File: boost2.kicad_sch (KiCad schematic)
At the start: 26 parts, among them Q6 BSC015NE2LS5I, Q7 BSC015NE2LS5I, U1 TPS43061

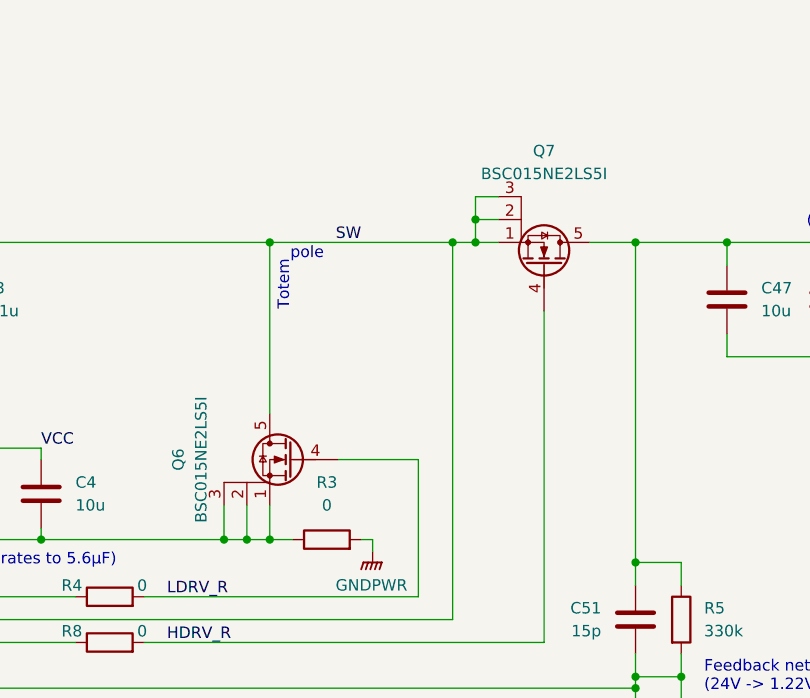
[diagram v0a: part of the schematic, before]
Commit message: Up charging current to 6A
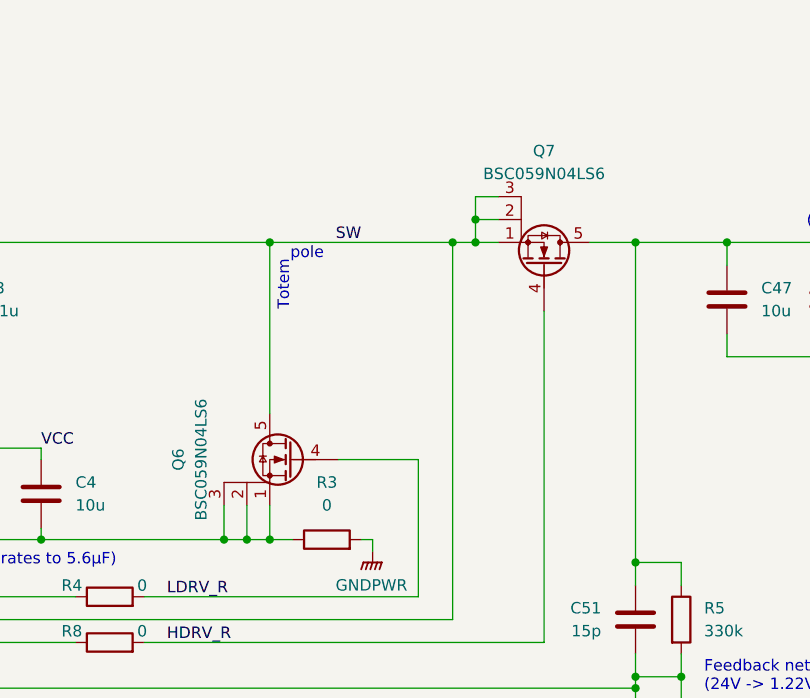
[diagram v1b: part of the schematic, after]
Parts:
- Q6, Q7: value BSC015NE2LS5I -> BSC059N04LS6; Mouser Part Number 726-BSC015NE2LS5IATM -> 726-BSC059N04LS6ATMA
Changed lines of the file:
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@@
 			)
 		)
-		(property "Value" "BSC015NE2LS5I"
+		(property "Value" "BSC059N04LS6"
 			(at 139.7 102.87 90)
 			(effects
@@
 			)
 		)
-		(property "Mouser Part Number" "726-BSC015NE2LS5IATM"
+		(property "Mouser Part Number" "726-BSC059N04LS6ATMA"
 			(at 149.86 102.87 0)
 			(effects
@@
 			)
 		)
-		(property "Value" "BSC015NE2LS5I"
+		(property "Value" "BSC059N04LS6"
 			(at 177.8 71.12 90)
 			(effects
@@
 			)
 		)
-		(property "Mouser Part Number" "726-BSC015NE2LS5IATM"
+		(property "Mouser Part Number" "726-BSC059N04LS6ATMA"
 			(at 177.8 81.28 0)
 			(effects

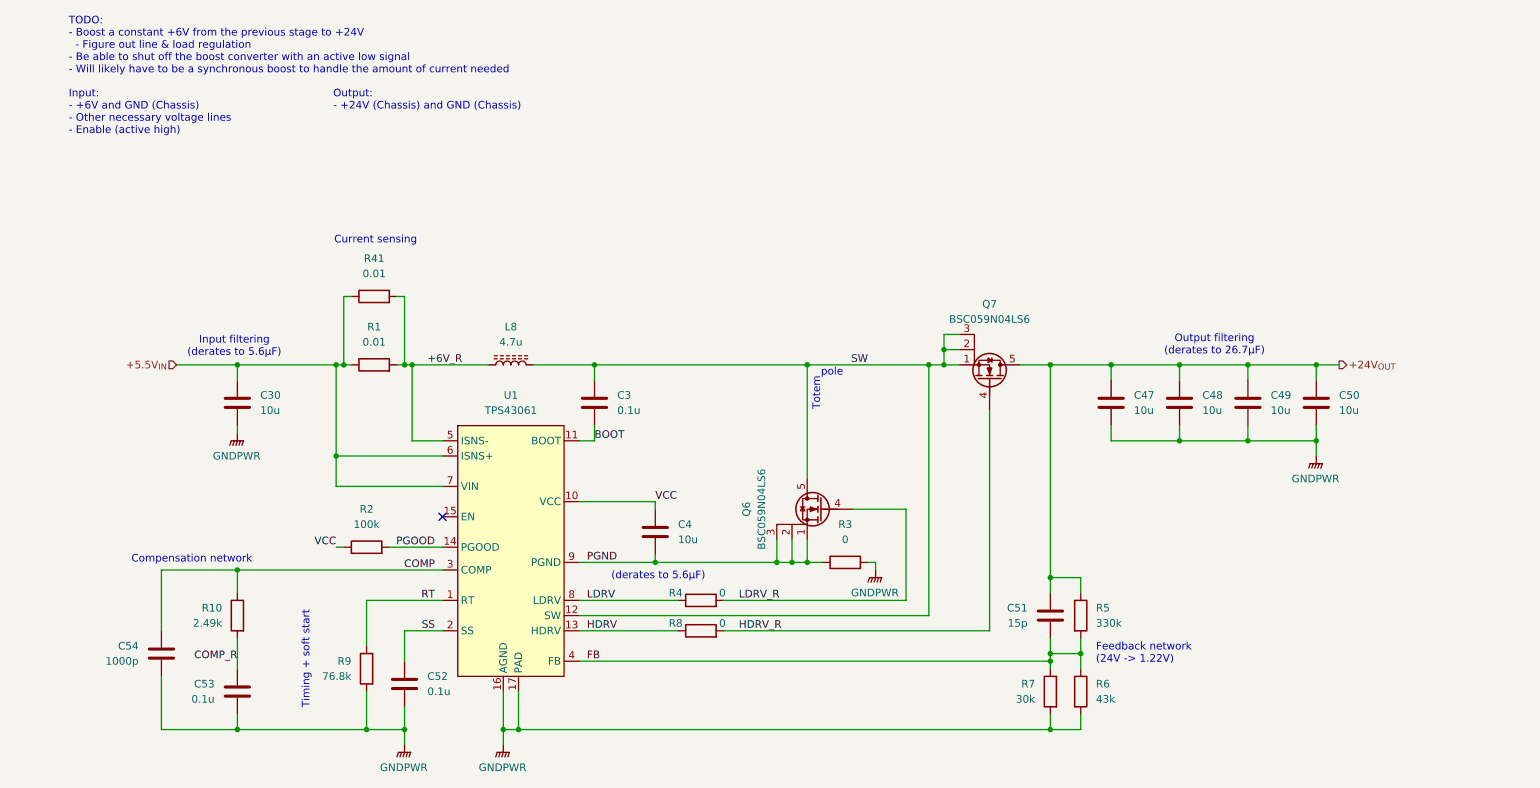
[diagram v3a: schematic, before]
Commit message: Reannotate schematic
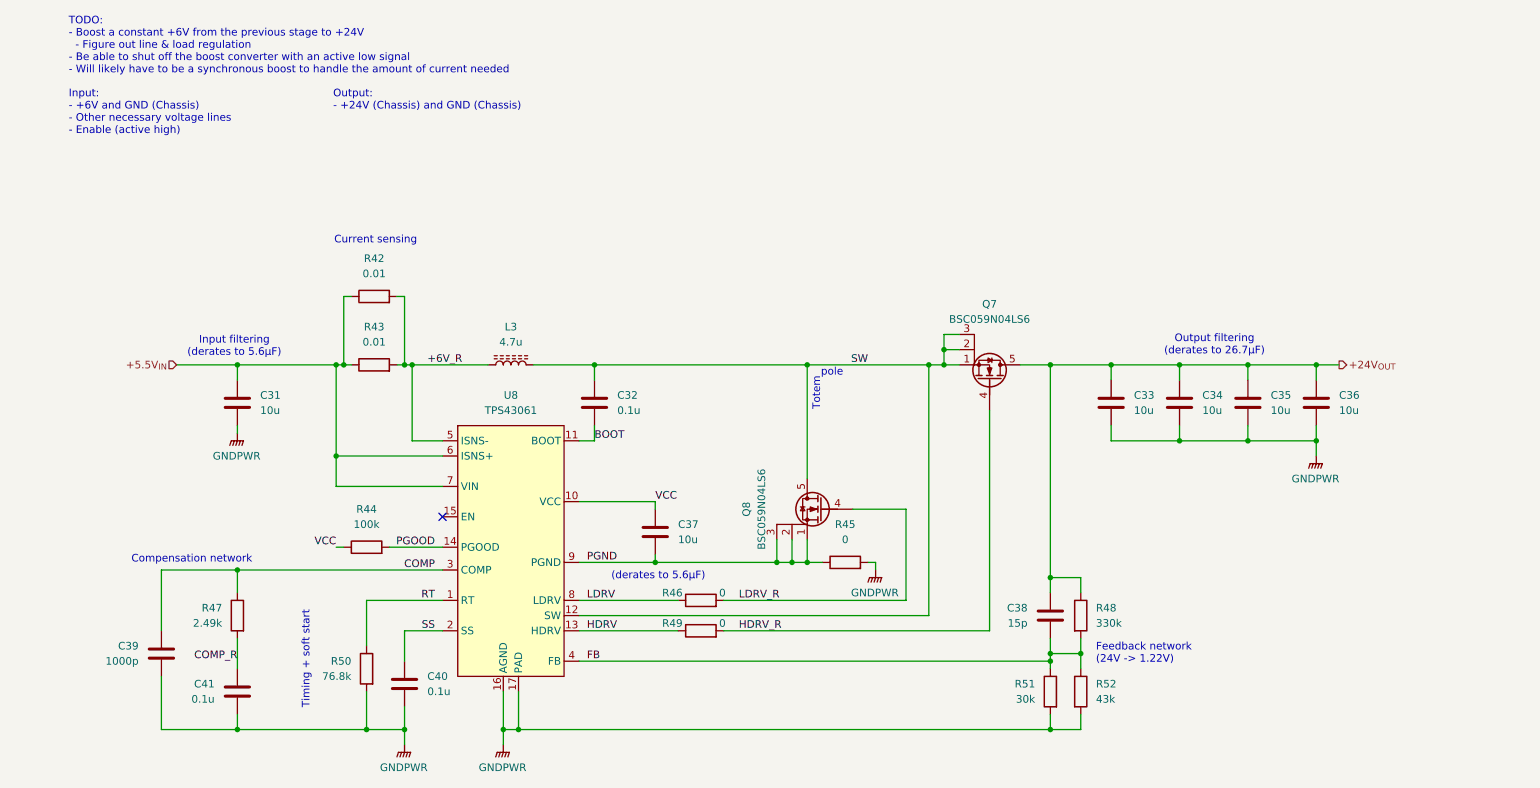
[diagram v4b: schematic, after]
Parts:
- renumbered C30 to C31, C3 to C32, C47 to C33, C48 to C34, C49 to C35, C50 to C36, C4 to C37, C51 to C38, C54 to C39, C52 to C40, C53 to C41, L8 to L3, Q6 to Q8, R41 to R42, R1 to R43, R2 to R44, R3 to R45, R4 to R46, R10 to R47, R5 to R48, R8 to R49, R9 to R50, R7 to R51, R6 to R52, U1 to U8
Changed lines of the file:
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@@
 		(dnp no)
 		(fields_autoplaced yes)
-		(property "Reference" "R3"
+		(property "Reference" "R45"
 			(at 153.67 105.41 90)
 			(effects
@@
 			(project "SupercapManager"
 				(path "/6197145b-e7d4-44cc-9d90-537b6501bf60/47dffa6f-2678-4be2-969a-7f2e7310ccad"
-					(reference "R3")
+					(reference "R45")
 					(unit 1)
 				)
@@
 		(dnp no)
 		(fields_autoplaced yes)
-		(property "Reference" "R2"
+		(property "Reference" "R44"
 			(at 73.66 102.87 90)
 			(effects
@@
 			(project ""
 				(path "/6197145b-e7d4-44cc-9d90-537b6501bf60/47dffa6f-2678-4be2-969a-7f2e7310ccad"
-					(reference "R2")
+					(reference "R44")
 					(unit 1)
 				)
@@
 		(dnp no)
 		(fields_autoplaced yes)
-		(property "Reference" "#PWR015"
+		(property "Reference" "#PWR053"
 			(at 52.07 95.25 0)
 			(effects
@@
 			(project "SupercapManager"
 				(path "/6197145b-e7d4-44cc-9d90-537b6501bf60/47dffa6f-2678-4be2-969a-7f2e7310ccad"
-					(reference "#PWR015")
+					(reference "#PWR053")
 					(unit 1)
 				)
@@
 		(dnp no)
 		(fields_autoplaced yes)
-		(property "Reference" "#PWR018"
+		(property "Reference" "#PWR057"
 			(at 96.52 147.32 0)
 			(effects
@@
 			(project "SupercapManager"
 				(path "/6197145b-e7d4-44cc-9d90-537b6501bf60/47dffa6f-2678-4be2-969a-7f2e7310ccad"
-					(reference "#PWR018")
+					(reference "#PWR057")
 					(unit 1)
 				)
@@
 		(dnp no)
 		(fields_autoplaced yes)
-		(property "Reference" "C52"
+		(property "Reference" "C40"
 			(at 83.82 130.8099 0)
 			(effects
@@
 			(project "SupercapManager"
 				(path "/6197145b-e7d4-44cc-9d90-537b6501bf60/47dffa6f-2678-4be2-969a-7f2e7310ccad"
-					(reference "C52")
+					(reference "C40")
 					(unit 1)
 				)
@@
 		(dnp no)
 		(fields_autoplaced yes)
-		(property "Reference" "R41"
+		(property "Reference" "R42"
 			(at 74.93 60.96 90)
 			(effects
@@
 			(project "SupercapManager"
 				(path "/6197145b-e7d4-44cc-9d90-537b6501bf60/47dffa6f-2678-4be2-969a-7f2e7310ccad"
-					(reference "R41")
+					(reference "R42")
 					(unit 1)
 				)
@@
 		(on_board yes)
 		(dnp no)
-		(property "Reference" "R7"
+		(property "Reference" "R51"
 			(at 185.42 132.0799 0)
 			(effects
@@
 			(project "SupercapManager"
 				(path "/6197145b-e7d4-44cc-9d90-537b6501bf60/47dffa6f-2678-4be2-969a-7f2e7310ccad"
-					(reference "R7")
+					(reference "R51")
 					(unit 1)
 				)
@@
 		(on_board yes)
 		(dnp no)
-		(property "Reference" "Q6"
+		(property "Reference" "Q8"
 			(at 137.16 102.87 90)
 			(effects
@@
 			(project "SupercapManager"
 				(path "/6197145b-e7d4-44cc-9d90-537b6501bf60/47dffa6f-2678-4be2-969a-7f2e7310ccad"
-					(reference "Q6")
+					(reference "Q8")
 					(unit 1)
 				)
@@
 		(dnp no)
 		(fields_autoplaced yes)
-		(property "Reference" "#PWR019"
+		(property "Reference" "#PWR056"
 			(at 80.01 147.32 0)
 			(effects
@@
 			(project "SupercapManager"
 				(path "/6197145b-e7d4-44cc-9d90-537b6501bf60/47dffa6f-2678-4be2-969a-7f2e7310ccad"
-					(reference "#PWR019")
+					(reference "#PWR056")
 					(unit 1)
 				)
@@
 		(on_board yes)
 		(dnp no)
-		(property "Reference" "R9"
+		(property "Reference" "R50"
 			(at 71.12 128.2699 0)
 			(effects
@@
 			(project "SupercapManager"
 				(path "/6197145b-e7d4-44cc-9d90-537b6501bf60/47dffa6f-2678-4be2-969a-7f2e7310ccad"
-					(reference "R9")
+					(reference "R50")
 					(unit 1)
 				)
@@
 		(on_board yes)
 		(dnp no)
-		(property "Reference" "R10"
+		(property "Reference" "R47"
 			(at 49.53 119.3799 0)
 			(effects
@@
 			(project "SupercapManager"
 				(path "/6197145b-e7d4-44cc-9d90-537b6501bf60/47dffa6f-2678-4be2-969a-7f2e7310ccad"
-					(reference "R10")
+					(reference "R47")
 					(unit 1)
 				)
@@
 		(dnp no)
 		(fields_autoplaced yes)
-		(property "Reference" "#PWR017"
+		(property "Reference" "#PWR054"
 			(at 232.41 99.06 0)
 			(effects
@@
 			(project "SupercapManager"
 				(path "/6197145b-e7d4-44cc-9d90-537b6501bf60/47dffa6f-2678-4be2-969a-7f2e7310ccad"
-					(reference "#PWR017")
+					(reference "#PWR054")
 					(unit 1)
 				)
@@
 		(on_board yes)
 		(dnp no)
-		(property "Reference" "C53"
+		(property "Reference" "C41"
 			(at 48.26 132.0799 0)
 			(effects
@@
 			(project "SupercapManager"
 				(path "/6197145b-e7d4-44cc-9d90-537b6501bf60/47dffa6f-2678-4be2-969a-7f2e7310ccad"
-					(reference "C53")
+					(reference "C41")
 					(unit 1)
 				)
@@
 		(on_board yes)
 		(dnp no)
-		(property "Reference" "R4"
+		(property "Reference" "R46"
 			(at 126.492 117.602 90)
 			(effects
@@
 			(project "SupercapManager"
 				(path "/6197145b-e7d4-44cc-9d90-537b6501bf60/47dffa6f-2678-4be2-969a-7f2e7310ccad"
-					(reference "R4")
+					(reference "R46")
 					(unit 1)
 				)
@@
 		(dnp no)
 		(fields_autoplaced yes)
-		(property "Reference" "C4"
+		(property "Reference" "C37"
 			(at 125.73 105.4099 0)
 			(effects
@@
 			(project "SupercapManager"
 				(path "/6197145b-e7d4-44cc-9d90-537b6501bf60/47dffa6f-2678-4be2-969a-7f2e7310ccad"
-					(reference "C4")
+					(reference "C37")
 					(unit 1)
 				)
@@
 		(dnp no)
 		(fields_autoplaced yes)
-		(property "Reference" "C50"
+		(property "Reference" "C36"
 			(at 236.22 83.8199 0)
 			(effects
@@
 			(project "SupercapManager"
 				(path "/6197145b-e7d4-44cc-9d90-537b6501bf60/47dffa6f-2678-4be2-969a-7f2e7310ccad"
-					(reference "C50")
+					(reference "C36")
 					(unit 1)
 				)
@@
 		(dnp no)
 		(fields_autoplaced yes)
-		(property "Reference" "C49"
+		(property "Reference" "C35"
 			(at 224.79 83.8199 0)
 			(effects
@@
 			(project "SupercapManager"
 				(path "/6197145b-e7d4-44cc-9d90-537b6501bf60/47dffa6f-2678-4be2-969a-7f2e7310ccad"
-					(reference "C49")
+					(reference "C35")
 					(unit 1)
 				)
@@
 		(dnp no)
 		(fields_autoplaced yes)
-		(property "Reference" "C48"
+		(property "Reference" "C34"
 			(at 213.36 83.8199 0)
 			(effects
@@
 			(project "SupercapManager"
 				(path "/6197145b-e7d4-44cc-9d90-537b6501bf60/47dffa6f-2678-4be2-969a-7f2e7310ccad"
-					(reference "C48")
+					(reference "C34")
 					(unit 1)
 				)
@@
 		(dnp no)
 		(fields_autoplaced yes)
-		(property "Reference" "U1"
+		(property "Reference" "U8"
 			(at 97.79 83.82 0)
 			(effects
@@
 			(project ""
 				(path "/6197145b-e7d4-44cc-9d90-537b6501bf60/47dffa6f-2678-4be2-969a-7f2e7310ccad"
-					(reference "U1")
+					(reference "U8")
 					(unit 1)
 				)
@@
 		(on_board yes)
 		(dnp no)
-		(property "Reference" "C51"
+		(property "Reference" "C38"
 			(at 184.15 119.3799 0)
 			(effects
@@
 			(project ""
 				(path "/6197145b-e7d4-44cc-9d90-537b6501bf60/47dffa6f-2678-4be2-969a-7f2e7310ccad"
-					(reference "C51")
+					(reference "C38")
 					(unit 1)
 				)
@@
 		(on_board yes)
 		(dnp no)
-		(property "Reference" "R8"
+		(property "Reference" "R49"
 			(at 126.492 122.682 90)
 			(effects
@@
 			(project "SupercapManager"
 				(path "/6197145b-e7d4-44cc-9d90-537b6501bf60/47dffa6f-2678-4be2-969a-7f2e7310ccad"
-					(reference "R8")
+					(reference "R49")
 					(unit 1)
 				)
@@
 		(dnp no)
 		(fields_autoplaced yes)
-		(property "Reference" "#PWR016"
+		(property "Reference" "#PWR055"
 			(at 158.75 118.11 0)
 			(effects
@@
 			(project ""
 				(path "/6197145b-e7d4-44cc-9d90-537b6501bf60/47dffa6f-2678-4be2-969a-7f2e7310ccad"
-					(reference "#PWR016")
+					(reference "#PWR055")
 					(unit 1)
 				)
@@
 		(dnp no)
 		(fields_autoplaced yes)
-		(property "Reference" "R1"
+		(property "Reference" "R43"
 			(at 74.93 72.39 90)
 			(effects
@@
 			(project ""
 				(path "/6197145b-e7d4-44cc-9d90-537b6501bf60/47dffa6f-2678-4be2-969a-7f2e7310ccad"
-					(reference "R1")
+					(reference "R43")
 					(unit 1)
 				)
@@
 		(dnp no)
 		(fields_autoplaced yes)
-		(property "Reference" "C3"
+		(property "Reference" "C32"
 			(at 115.57 83.8199 0)
 			(effects
@@
 			(project ""
 				(path "/6197145b-e7d4-44cc-9d90-537b6501bf60/47dffa6f-2678-4be2-969a-7f2e7310ccad"
-					(reference "C3")
+					(reference "C32")
 					(unit 1)
 				)
@@
 		(on_board yes)
 		(dnp no)
-		(property "Reference" "C47"
+		(property "Reference" "C33"
 			(at 201.93 83.8199 0)
 			(effects
@@
 			(project ""
 				(path "/6197145b-e7d4-44cc-9d90-537b6501bf60/47dffa6f-2678-4be2-969a-7f2e7310ccad"
-					(reference "C47")
+					(reference "C33")
 					(unit 1)
 				)
@@
 		(dnp no)
 		(fields_autoplaced yes)
-		(property "Reference" "R6"
+		(property "Reference" "R52"
 			(at 195.58 132.0799 0)
 			(effects
@@
 			(project "SupercapManager"
 				(path "/6197145b-e7d4-44cc-9d90-537b6501bf60/47dffa6f-2678-4be2-969a-7f2e7310ccad"
-					(reference "R6")
+					(reference "R52")
 					(unit 1)
 				)
@@
 		(dnp no)
 		(fields_autoplaced yes)
-		(property "Reference" "L8"
+		(property "Reference" "L3"
 			(at 97.79 72.39 90)
 			(effects
@@
 			(project ""
 				(path "/6197145b-e7d4-44cc-9d90-537b6501bf60/47dffa6f-2678-4be2-969a-7f2e7310ccad"
-					(reference "L8")
+					(reference "L3")
 					(unit 1)
 				)
@@
 		(on_board yes)
 		(dnp no)
-		(property "Reference" "C54"
+		(property "Reference" "C39"
 			(at 35.56 125.7299 0)
 			(effects
@@
 			(project "SupercapManager"
 				(path "/6197145b-e7d4-44cc-9d90-537b6501bf60/47dffa6f-2678-4be2-969a-7f2e7310ccad"
-					(reference "C54")
+					(reference "C39")
 					(unit 1)
 				)
@@
 		(dnp no)
 		(fields_autoplaced yes)
-		(property "Reference" "C30"
+		(property "Reference" "C31"
 			(at 55.88 83.8199 0)
 			(effects
@@
 			(project "SupercapManager"
 				(path "/6197145b-e7d4-44cc-9d90-537b6501bf60/47dffa6f-2678-4be2-969a-7f2e7310ccad"
-					(reference "C30")
+					(reference "C31")
 					(unit 1)
 				)
@@
 		(dnp no)
 		(fields_autoplaced yes)
-		(property "Reference" "R5"
+		(property "Reference" "R48"
 			(at 195.58 119.3799 0)
 			(effects
@@
 			(project ""
 				(path "/6197145b-e7d4-44cc-9d90-537b6501bf60/47dffa6f-2678-4be2-969a-7f2e7310ccad"
-					(reference "R5")
+					(reference "R48")
 					(unit 1)
 				)

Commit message: Finalized design !!!
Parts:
- removed C31: 10u, Capacitor_SMD:C_0805_2012Metric_Pad1.18x1.45mm_HandSolder, symbol Device:C
- removed C33, C34: 10u, Capacitor_SMD:C_1206_3216Metric_Pad1.33x1.80mm_HandSolder, symbol Device:C
- removed R42: 0.01, Resistor_SMD:R_0612_1632Metric_Pad1.18x3.40mm_HandSolder, symbol Device:R
- added C31, C33, C34: 220u, Capacitor_THT:CP_Radial_D6.3mm_P2.50mm, symbol Device:C_Polarized
- added C75: 0.1u, Capacitor_SMD:C_0603_1608Metric_Pad1.08x0.95mm_HandSolder, symbol Device:C
- added R78: 1m, Resistor_SMD:R_0612_1632Metric_Pad1.18x3.40mm_HandSolder, symbol Device:R
- added R79: 47m, Resistor_SMD:R_1206_3216Metric_Pad1.30x1.75mm_HandSolder, symbol Device:R
- C35, C36: value 10u -> 1u; footprint Capacitor_SMD:C_1206_3216Metric_Pad1.33x1.80mm_HandSolder -> Capacitor_SMD:C_0603_1608Metric_Pad1.08x0.95mm_HandSolder; Mouser Part Number 187-CL31A106MBHNNNE -> (none)
- C39: value 1000p -> 180p
- C41: value 0.1u -> 0.01u
- L3: value 4.7u -> 1.5u; footprint Inductor_SMD:L_Bourns_SRN8040TA -> Inductor_SMD:L_Bourns_SRP1245A; Mouser Part Number 652-SRN8040TA-4R7M -> 652-SRP1265A-1R8M
- R43: value 0.01 -> 1m; Mouser Part Number 652-CFG0612FXR010ELF -> 71-WFCP06121L000FE66
- R47: value 2.49k -> 22.6k
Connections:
- net +24V_{OUT}: now also C33.1, C34.1
- net GNDPWR: now also C31.2, C33.2, C34.2, C75.2
- net +5.5V_{IN} renamed IN
- net IN: now also C31.1, C75.1, R78.1, R79.1; no longer R43.1
- net +6V_R renamed ISNS-
- net ISNS-: now also R79.2
- new net IN_R: R43.1, R78.2
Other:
- note added: "Input filtering"
- note added: "Output filtering"
- note removed: "Input filtering (derates to 5.6µF)"
- note removed: "Output filtering (derates to 26.7µF)"
